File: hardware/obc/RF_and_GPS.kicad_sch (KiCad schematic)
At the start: 10 parts, among them J601 Conn_01x08_Socket, J602 SMA RA Connector, J603 SMA RA Connector, J604 SMA RA Connector, U601 RFM98PW, U602 S1216V8, U603 GP2S1+

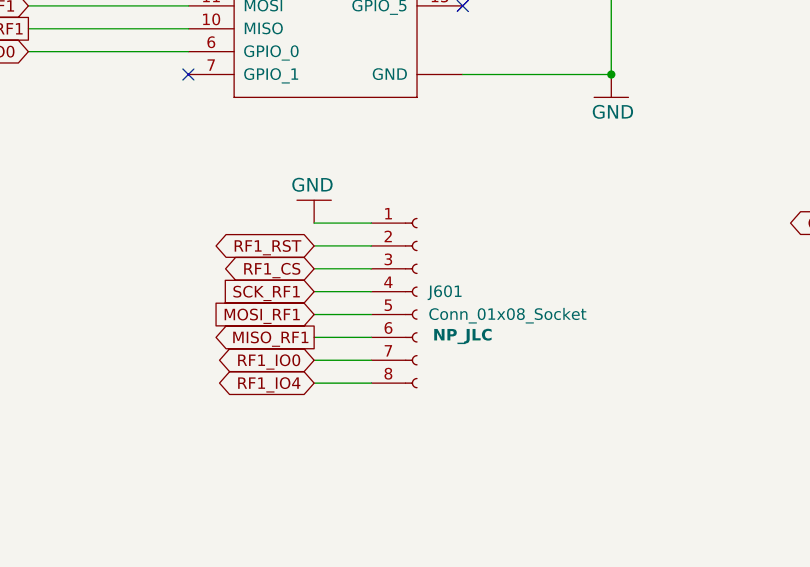
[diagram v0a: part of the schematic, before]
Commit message: obc: Updates from 6/28 design review and small fixes
- various board layout work to clear DRC errors, better connect planes,
delete hanging tracks, etc.
- Set radio thermal hole net names to eliminate DRC errors
- Straightened some traces and improved clearances
- Migrated legacy format symbol library mainboard.lib ->
mainboard.kicad_sym.  Still needs unification with other NyanSat
symbol libraries.
- Renumbered LTC4121 symbol pins from e.g. P$1 to just '1' to match
KiCad conventions.
- Moved LTC4121 to KiCad QFN 16 0.5 built-in symbol
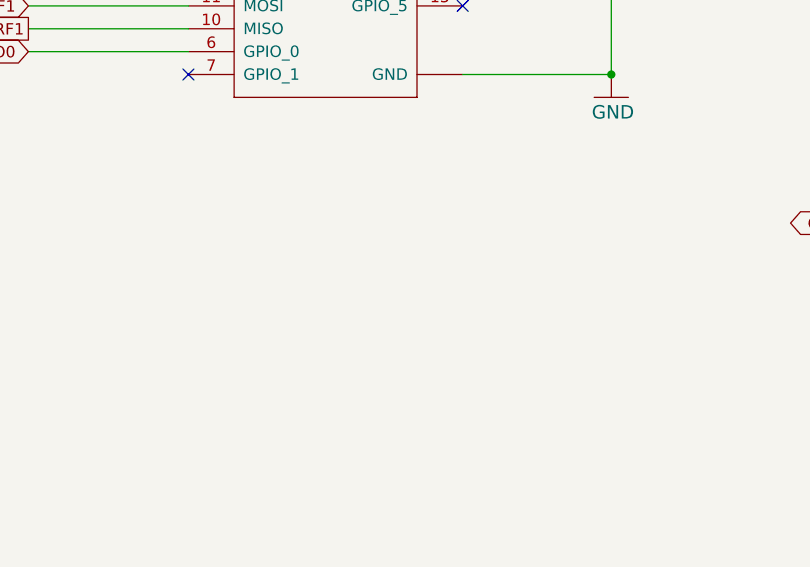
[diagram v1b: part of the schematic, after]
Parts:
- removed J601: Conn_01x08_Socket, Connector_PinSocket_2.54mm:PinSocket_1x08_P2.54mm_Vertical, symbol Connector:Conn_01x08_Socket

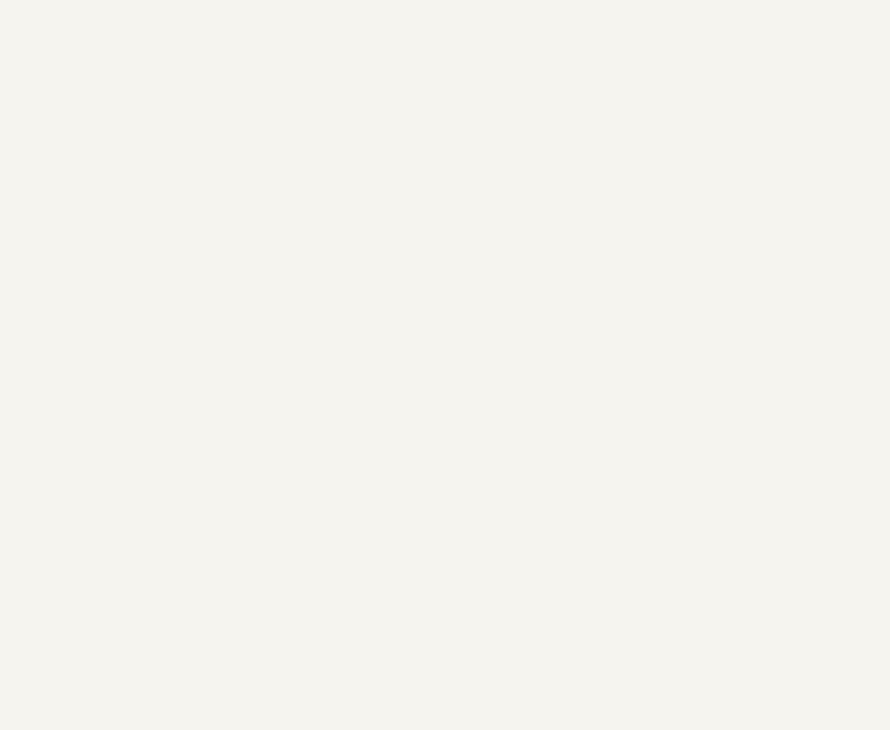
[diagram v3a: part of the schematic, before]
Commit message: Hardware/OBC: Added RP2350B and edited schematics
- Added RP2350B
	- Pinned all GPIOs
- Added Decoupling
- Added Crystal
- Started adding MRAM
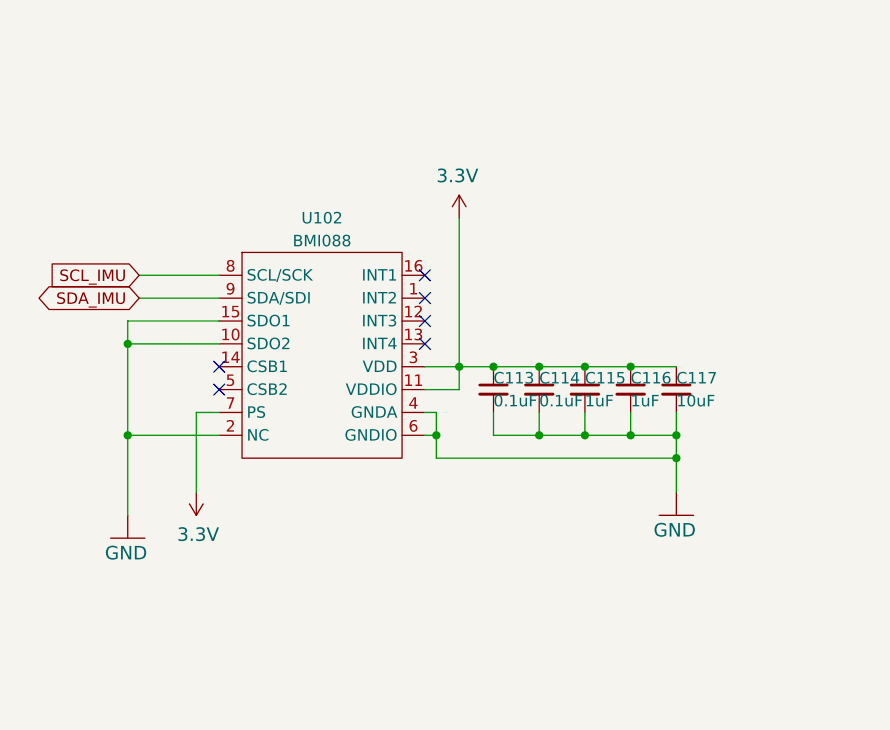
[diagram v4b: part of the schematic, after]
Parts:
- added C113, C114: 0.1uF, Capacitor_SMD:C_0603_1608Metric, symbol mainboard:C_Small
- added C115, C116: 1uF, Capacitor_SMD:C_0603_1608Metric, symbol mainboard:C_Small
- added C117: 10uF, Capacitor_SMD:C_0603_1608Metric, symbol mainboard:C_Small
- added U102: BMI088, SSE_Footprints:LGA-16_4.5x3.0mm_P0.5mm, symbol SSE_Symbols:IMU_BMI088
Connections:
- net 3.3V: now also C113.1, C114.1, C115.1, C116.1, C117.1, U102.11 (VDDIO), U102.3 (VDD), U102.7 (PS)
- net GND: now also C113.2, C114.2, C115.2, C116.2, C117.2, U102.10 (SDO2), U102.15 (SDO1), U102.2 (NC), U102.4 (GNDA), U102.6 (GNDIO)
- new net SCL_IMU: U102.8 (SCL/SCK)
- new net SDA_IMU: U102.9 (SDA/SDI)
- no-connect marks 18 -> 24

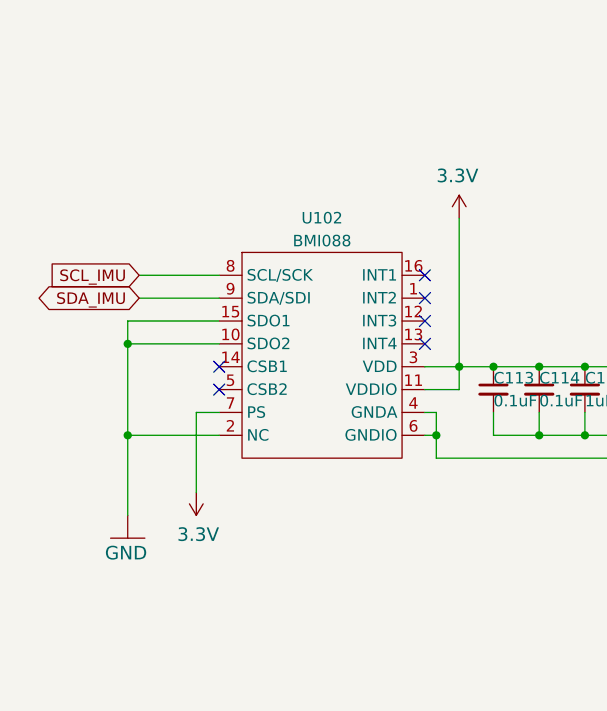
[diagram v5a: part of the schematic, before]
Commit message: OBC: Continuing work towards the next revision
- tidied up Radio and GPS page
- moved J305 to Avionics page
- changed R423 to 1.5k
- removed R428 so ILIM pin connects directly to GNDREF
- changed L403 to 4.7uH
- deleted BOM fields proto and flight
- connected C130 to ground
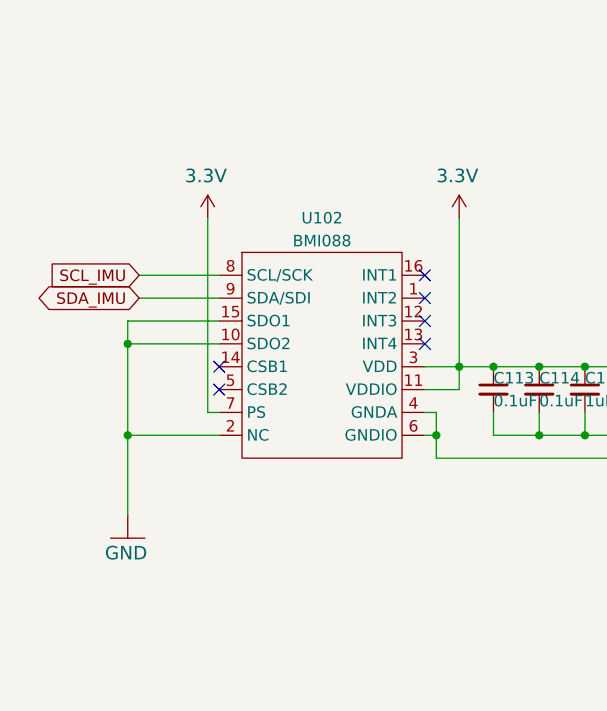
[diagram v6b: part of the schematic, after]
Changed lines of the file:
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@@
 	(wire
 		(pts
-			(xy 49.53 142.24) (xy 49.53 133.35)
+			(xy 50.8 111.76) (xy 50.8 133.35)
 		)
 		(stroke
@@
 	(wire
 		(pts
-			(xy 49.53 133.35) (xy 52.07 133.35)
+			(xy 50.8 133.35) (xy 52.07 133.35)
 		)
 		(stroke
@@
 	(symbol
 		(lib_id "mainboard:3.3V")
-		(at 49.53 142.24 180)
+		(at 50.8 111.76 0)
 		(unit 1)
 		(exclude_from_sim no)
@@
 		(dnp no)
 		(property "Reference" "#SUPPLY0108"
-			(at 49.53 142.24 0)
+			(at 50.8 111.76 0)
 			(effects
 				(font
@@
 		)
 		(property "Value" "3.3V"
-			(at 52.07 146.05 0)
+			(at 48.26 107.95 0)
 			(effects
 				(font
@@
 		)
 		(property "Footprint" ""
-			(at 49.53 142.24 0)
+			(at 50.8 111.76 0)
 			(effects
 				(font
@@
 		)
 		(property "Datasheet" ""
-			(at 49.53 142.24 0)
+			(at 50.8 111.76 0)
 			(effects
 				(font
@@
 		)
 		(property "Description" ""
-			(at 49.53 142.24 0)
-			(effects
-				(font
+			(at 50.8 111.76 0)
+			(effects
+				(font

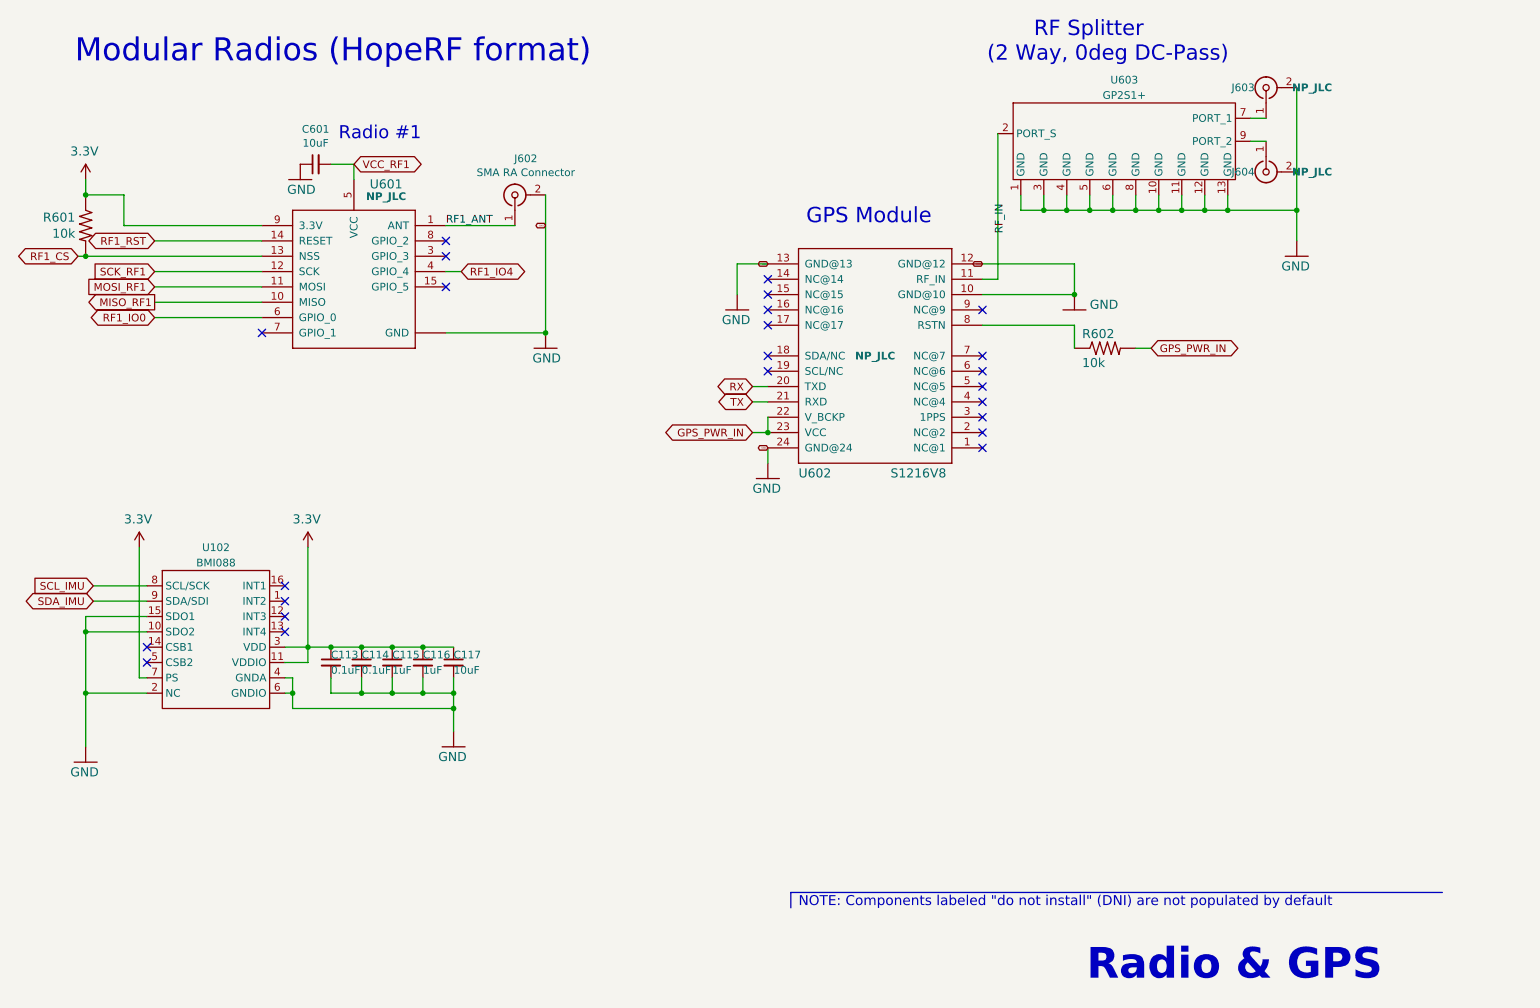
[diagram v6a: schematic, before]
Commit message: OBC: Continuing work towards the next revision
- Changed 3.3V names on Avionics page
- Removed buss protection-bypass jumpers
- Edited SPI buss protection
- Removed U302
- Removed JP401
- Other label/clean up modifications
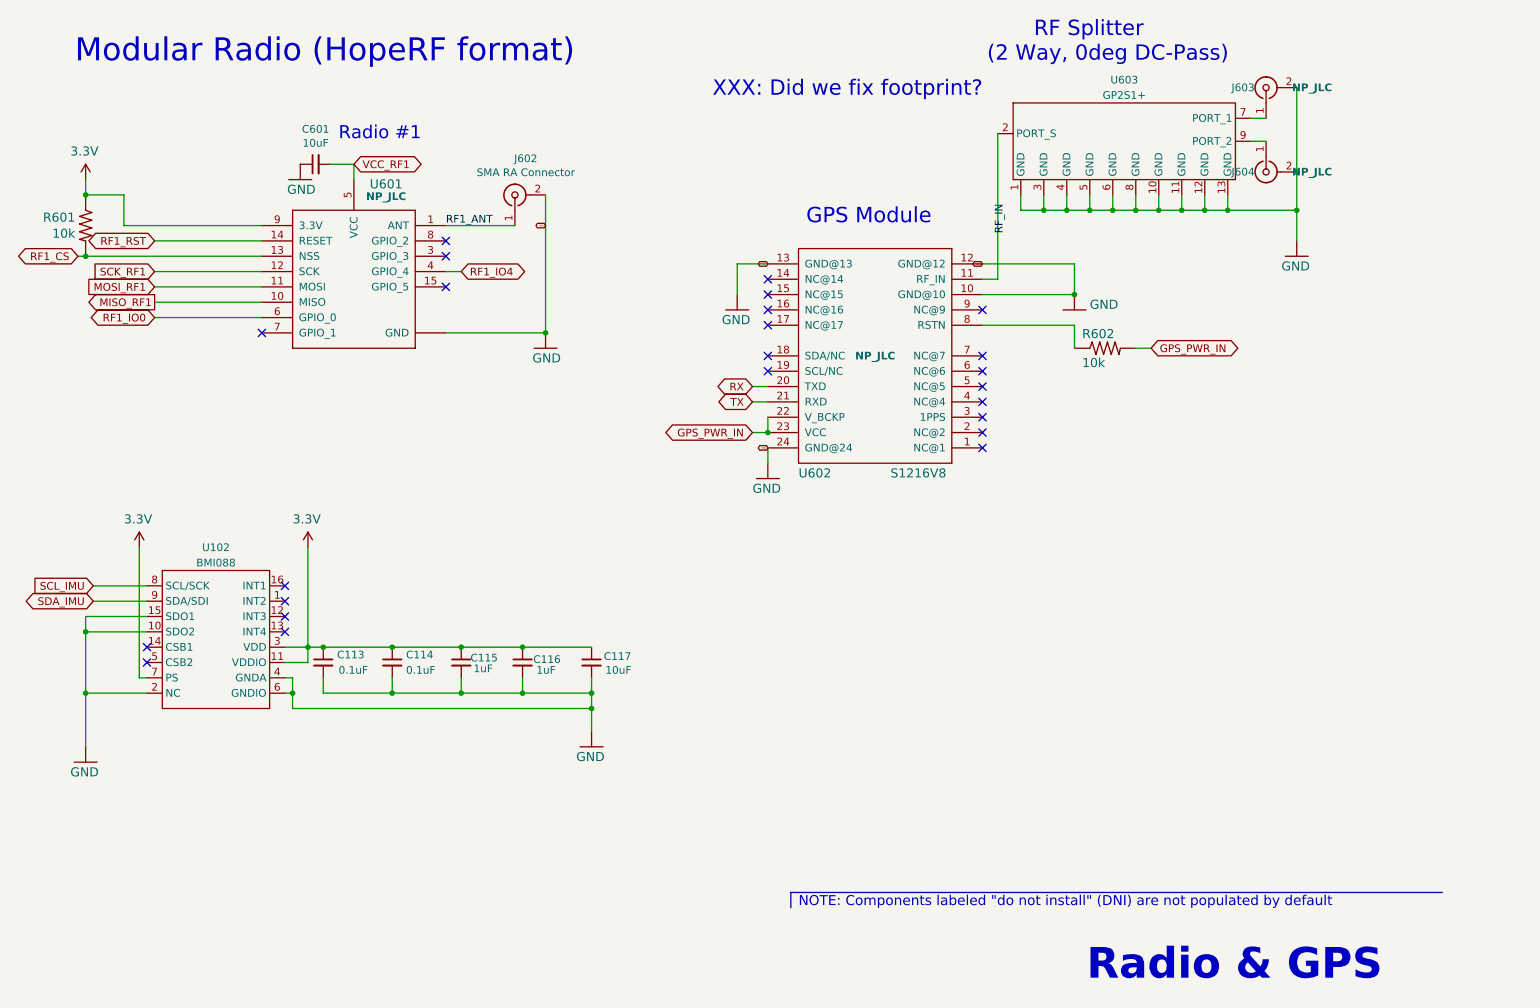
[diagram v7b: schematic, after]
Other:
- note added: "Modular Radio (HopeRF format)"
- note added: "XXX: Did we fix footprint?"
- note removed: "Modular Radios (HopeRF format)"
- moved on the sheet: C113, C114, C115, C116, C117
